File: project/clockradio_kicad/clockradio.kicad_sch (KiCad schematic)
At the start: 9 parts, among them SW1 RotaryEncoder_Switch, U1 RPi_Pico_TH

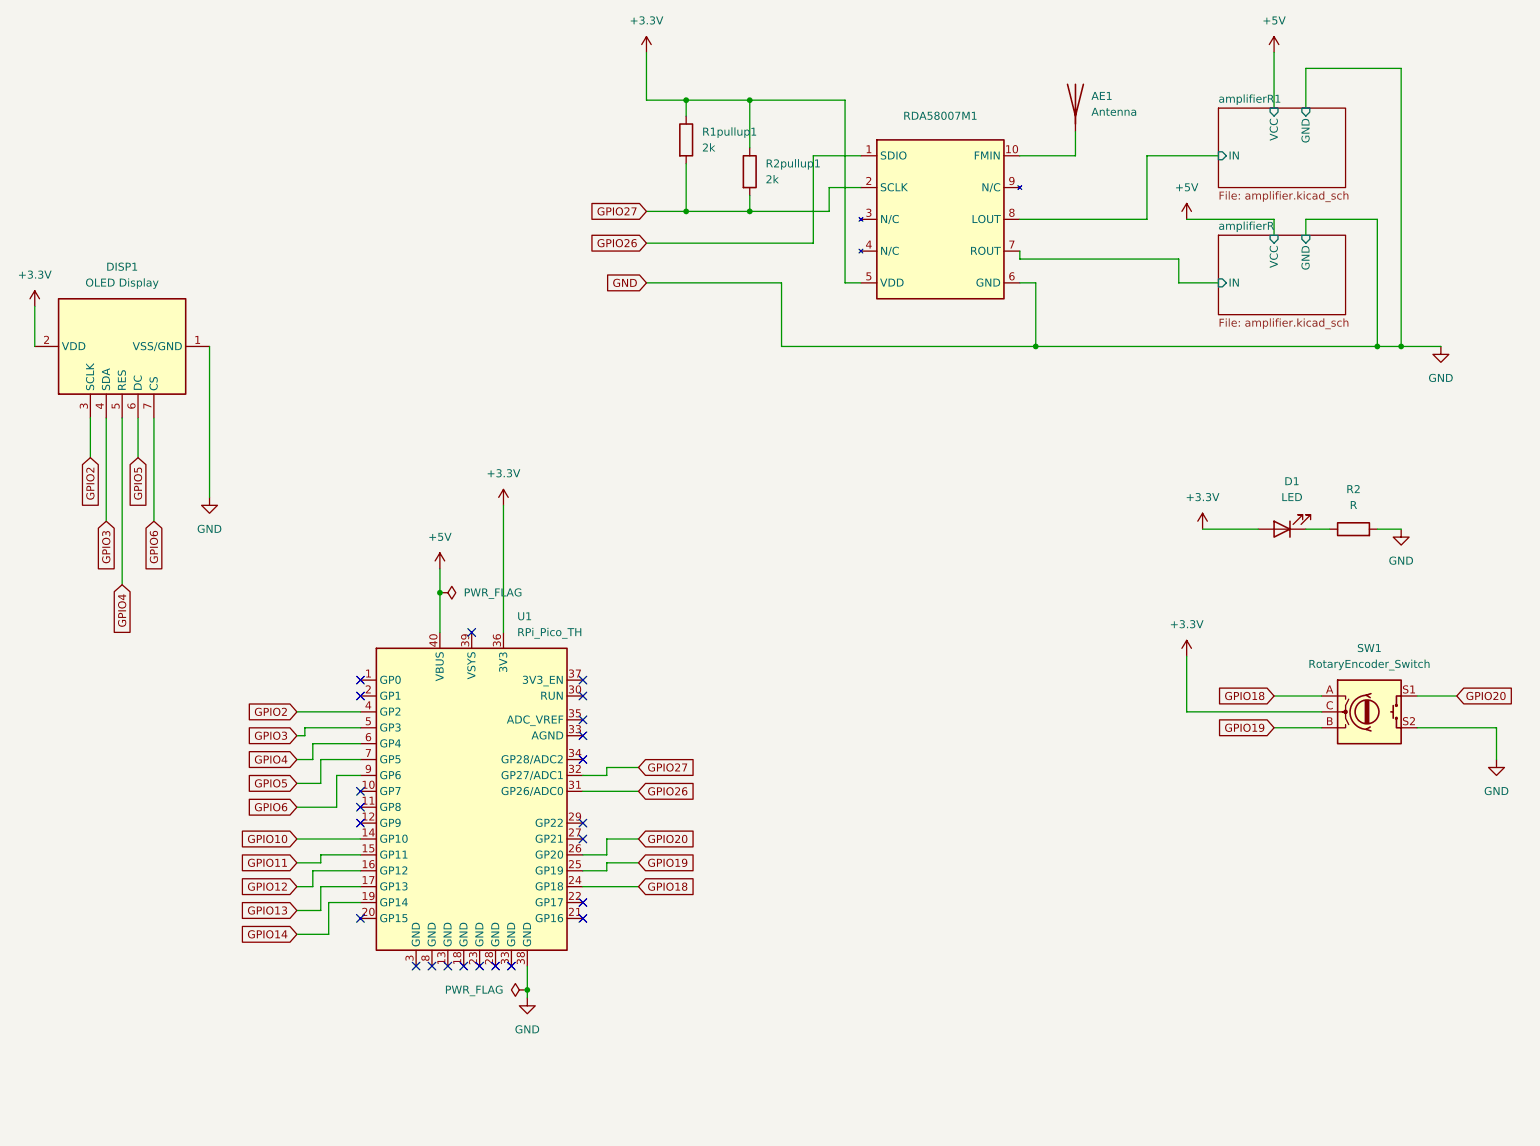
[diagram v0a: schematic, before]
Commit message: Add alarm sound schematic
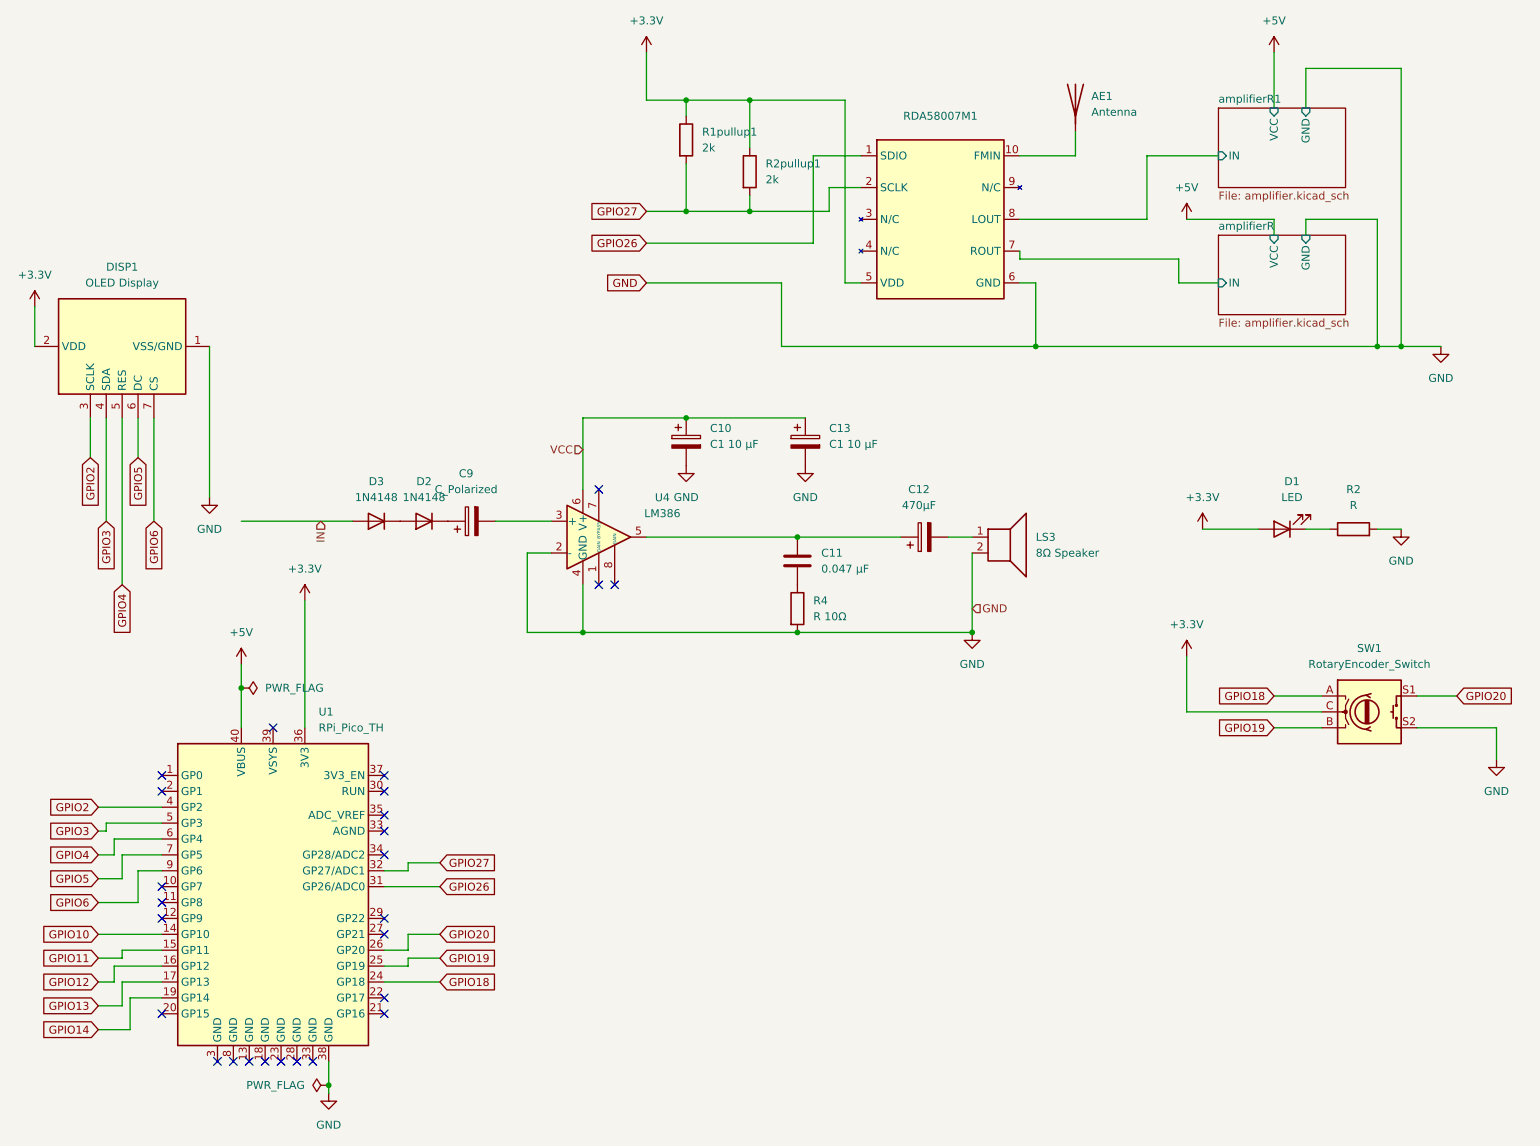
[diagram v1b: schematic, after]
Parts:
- added C10, C13: C1 10 µF, symbol Device:C_Polarized
- added C11: 0.047 µF, symbol Device:C
- added C12: 470µF, symbol Device:C_Polarized
- added C9: C_Polarized, symbol Device:C_Polarized
- added D2, D3: 1N4148, Diode_THT:D_DO-35_SOD27_P7.62mm_Horizontal, symbol Diode:1N4148
- added LS3: 8Ω Speaker, symbol Device:Speaker
- added R4: R 10Ω, Resistor_THT:R_Axial_DIN0309_L9.0mm_D3.2mm_P12.70mm_Horizontal, symbol Device:R
- added U4: LM386, ECE:DIP08, symbol Amplifier_Audio:LM386
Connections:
- net GND: now also C10.2, C13.2, LS3.2, R4.2, U4.2 (-), U4.4 (GND)
- new net: C11.1, C12.1, U4.5
- new net: C12.2, LS3.1
- new net: C11.2, R4.1
- new net: C9.1, D2.1 (K)
- new net: C9.2, U4.3 (+)
- new net: D2.2 (A), D3.1 (K)
- new net IN: D3.2 (A)
- new net VCC: C10.1, C13.1, U4.6 (V+)
- no-connect marks 23 -> 26
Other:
- moved on the sheet: U1

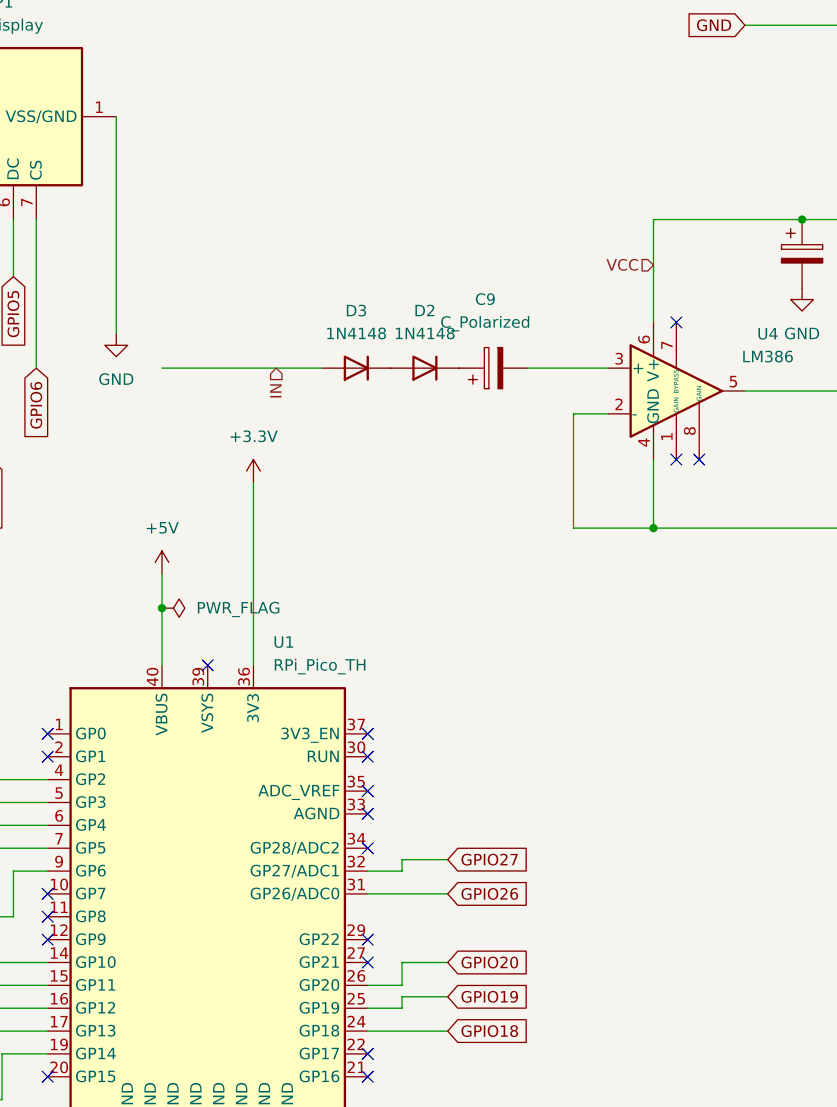
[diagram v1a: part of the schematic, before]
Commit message: Add global label for GPIO22 on alarm circuit
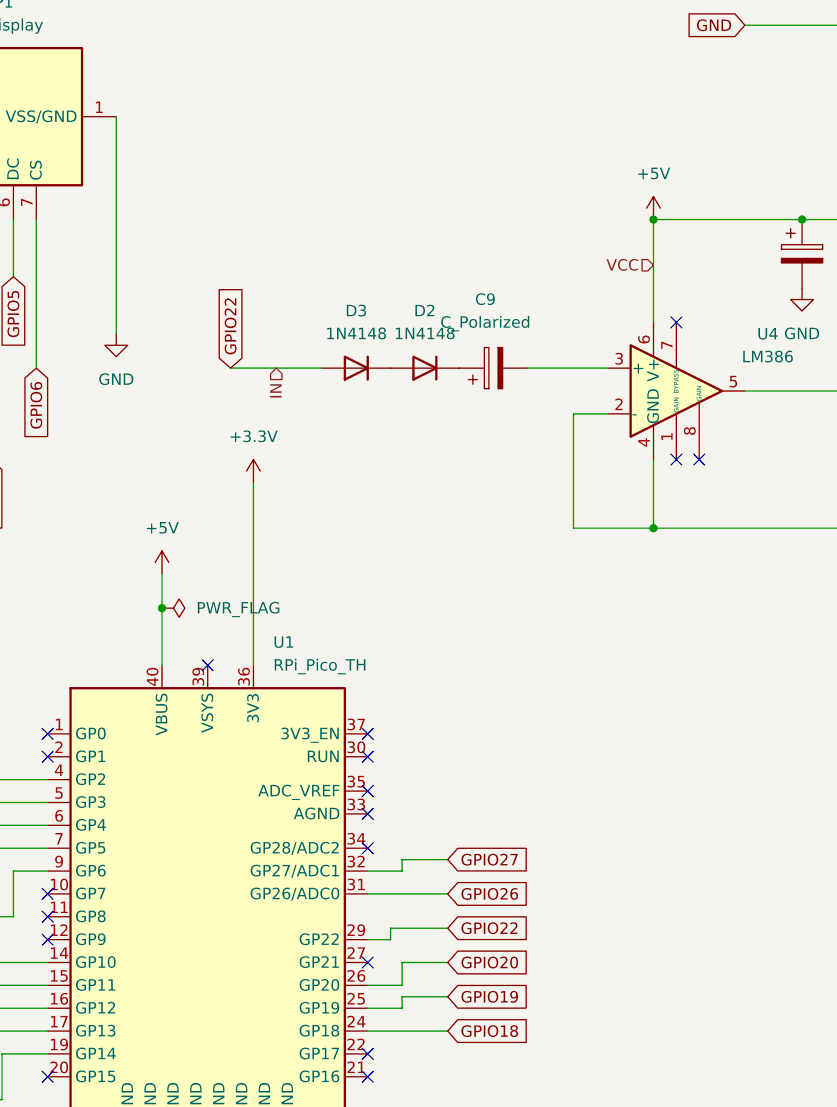
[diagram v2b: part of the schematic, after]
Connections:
- net IN is gone; now on net GPIO22: D3.2 (A)
- net VCC is gone; now on net +5V: C10.1, C13.1, U4.6 (V+)
- net GPIO22: now reaches U1.29 (GP22)
- no-connect marks 26 -> 25
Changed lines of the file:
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@@
 	)
 	(junction
+		(at 107.95 77.47)
+		(diameter 0)
+		(color 0 0 0 0)
+	)
+	(junction
 		(at 180.34 66.04)
 		(diameter 0)
@@
 	)
 	(no_connect
-		(at 76.2 157.48)
-	)
-	(no_connect
 		(at 76.2 147.32)
 	)
@@
 	(wire
 		(pts
+			(xy 78.74 156.21) (xy 85.09 156.21)
+		)
+		(stroke
+			(width 0)
+			(type default)
+		)
+	)
+	(wire
+		(pts
 			(xy 40.64 165.1) (xy 33.02 165.1)
 		)
@@
 	(wire
 		(pts
-			(xy 107.95 77.47) (xy 107.95 88.9)
+			(xy 60.96 93.98) (xy 71.12 93.98)
 		)
 		(stroke
@@
 	(wire
 		(pts
-			(xy 144.78 35.56) (xy 152.4 35.56)
+			(xy 107.95 77.47) (xy 107.95 88.9)
 		)
 		(stroke
@@
 	(wire
 		(pts
-			(xy 177.8 52.07) (xy 203.2 52.07)
+			(xy 144.78 35.56) (xy 152.4 35.56)
 		)
 		(stroke
@@
 	(wire
 		(pts
-			(xy 67.31 180.34) (xy 67.31 184.15)
+			(xy 177.8 52.07) (xy 203.2 52.07)
 		)
 		(stroke
@@
 	(wire
 		(pts
-			(xy 53.34 93.98) (xy 71.12 93.98)
+			(xy 67.31 180.34) (xy 67.31 184.15)
 		)
 		(stroke
@@
 	(wire
 		(pts
+			(xy 78.74 157.48) (xy 78.74 156.21)
+		)
+		(stroke
+			(width 0)
+			(type default)
+		)
+	)
+	(wire
+		(pts
+			(xy 76.2 157.48) (xy 78.74 157.48)
+		)
+		(stroke
+			(width 0)
+			(type default)
+		)
+	)
+	(wire
+		(pts
 			(xy 67.31 184.15) (xy 67.31 185.42)
 		)
@@
 		)
 	)
+	(global_label "GPIO22"
+		(shape input)
+		(at 85.09 156.21 0)
+		(fields_autoplaced yes)
+		(effects
+			(font
+				(size 1.27 1.27)
+			)
+			(justify left)
+		)
+		(property "Intersheetrefs" "${INTERSHEET_REFS}"
+			(at 94.9695 156.21 0)
+			(effects
+				(font
+					(size 1.27 1.27)
+				)
+				(justify left)
+				(hide yes)
+			)
+		)
+	)
 	(global_label "GPIO27"
 		(shape input)
@@
 		)
 	)
+	(global_label "GPIO22"
+		(shape input)
+		(at 60.96 93.98 90)
+		(fields_autoplaced yes)
+		(effects
+			(font
+				(size 1.27 1.27)
+			)
+			(justify left)
+		)
+		(property "Intersheetrefs" "${INTERSHEET_REFS}"
+			(at 60.96 86.0358 90)
+			(effects
+				(font
+					(size 1.27 1.27)
+				)
+				(justify left)
+				(hide yes)
+			)
+		)
+	)
 	(global_label "GPIO5"
 		(shape input)
@@
 					(unit 1)
 				)
+			)
+		)
+	)
+	(symbol
+		(lib_id "power:+5V")
+		(at 107.95 77.47 0)
+		(unit 1)
+		(exclude_from_sim no)
+		(in_bom yes)
+		(on_board yes)
+		(dnp no)
+		(fields_autoplaced yes)
+		(property "Reference" "#PWR018"
+			(at 107.95 81.28 0)
+			(effects
+				(font
+					(size 1.27 1.27)
+				)
+				(hide yes)
+			)
+		)
+		(property "Value" "+5V"
+			(at 107.95 72.39 0)
+			(effects
+				(font
+					(size 1.27 1.27)
+				)
+			)
+		)
+		(property "Footprint" ""
+			(at 107.95 77.47 0)
+			(effects
+				(font
+					(size 1.27 1.27)
+				)
+				(hide yes)
+			)
+		)
+		(property "Datasheet" ""
+			(at 107.95 77.47 0)
+			(effects
+				(font
+					(size 1.27 1.27)
+				)
+				(hide yes)
+			)
+		)
+		(property "Description" "Power symbol creates a global label with name \"+5V\""
+			(at 107.95 77.47 0)
+			(effects
+				(font
+					(size 1.27 1.27)
+				)
+				(hide yes)
+			)
+		)
+		(pin "1"
+		)
+		(instances
+			(project ""
+				(path "/26cce7b5-0449-425b-905b-3af383c44d12"
+					(reference "#PWR018")
+					(unit 1)
+				)
